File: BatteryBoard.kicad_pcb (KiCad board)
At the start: 4 copper layers, 18 parts, among them SW1 SW_SPST, U1 BQ25619ERTWR

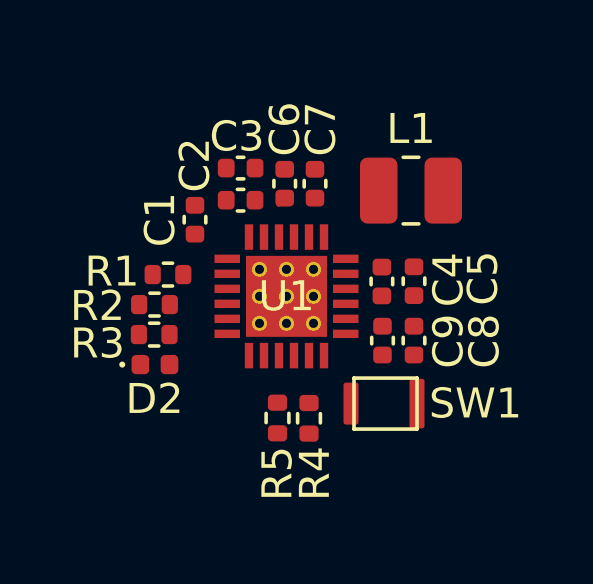
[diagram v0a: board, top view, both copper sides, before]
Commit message: Board Outline and placement Completed
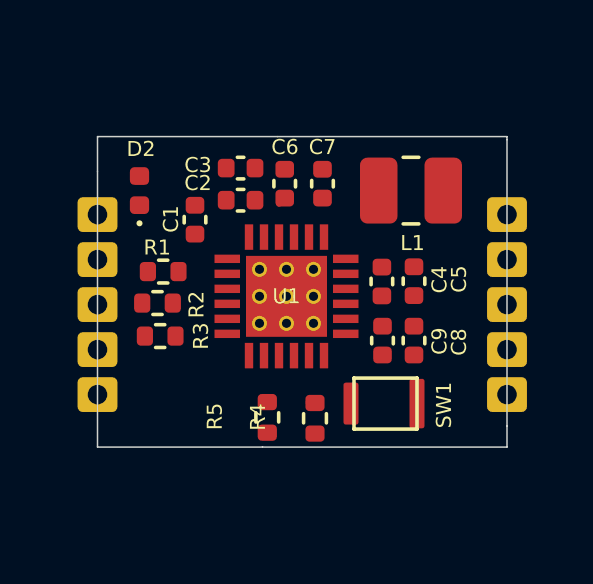
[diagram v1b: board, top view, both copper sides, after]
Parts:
- added J1: Conn_01x05_Pin, Library:5_Castellated, F.Cu at (67.1, 43.4)
- added J2: Conn_01x05_Pin, Library:5_Castellated, F.Cu at (80.8, 43.4)
- moved D2 5.82 mm to (68.5, 42.6), turned to 90 degrees
- moved R5 0.34 mm to (72.8, 50.2)
- moved C7 0.25 mm to (74.6, 42.4), turned to 90 degrees
- moved R3 0.21 mm to (69.2, 47.5)
- moved R4 0.20 mm to (74.3, 50.2)
- moved R1 0.19 mm to (69.3, 45.3)
- moved R2 0.11 mm to (69.1, 46.4)
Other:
- board outline added: 13.7 x 10.4 mm

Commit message: Minor Update for Routing
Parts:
- removed D2: LED, LED_SMD:LED_0402_1005Metric
- removed R3: 10k, Resistor_SMD:R_0402_1005Metric
- moved R4 1.98 mm to (72.4, 50.0), turned to 0 degrees
- moved R5 1.57 mm to (74.3, 50.0), turned to 0 degrees
- moved R2 1.23 mm to (69.5, 47.5), turned to -90 degrees
- moved J1 0.50 mm to (67.6, 43.4)
- moved R1 0.34 mm to (69.6, 45.5), turned to -90 degrees
- moved SW1 0.21 mm to (77.9, 49.6)
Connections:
- U1 pad 3: /PG -> unconnected-(U1-PMID_GOOD-Pad3)
- U1 pad 4: /STAT -> unconnected-(U1-STAT-Pad4)
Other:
- board size 13.7 x 10.4 mm -> 13.2 x 10.4 mm

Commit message: Out to Review
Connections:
- C7 pad 1: Net-(C7-Pad1) -> /SW
- J2 pad 4: Net-(J2-Pin_4) -> /BUTTON
- J2 pad 5: /SW -> /TS_BAT
- L1 pad 1: Net-(C7-Pad1) -> /SW
- R5 pad 2: Net-(J2-Pin_4) -> /TS_BAT
- SW1 pad 2: /SW -> /BUTTON
- U1 pad 12: /SW -> /BUTTON
- U1 pad 19: Net-(C7-Pad1) -> /SW
- U1 pad 20: Net-(C7-Pad1) -> /SW
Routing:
- net /VBAT: track 0.00 -> 12.2 mm, vias 0 -> 2
- net VBUS: track 0.00 -> 12.1 mm
- net /VSYS: track 0.00 -> 10.7 mm
- net GND: track 0.00 -> 8.44 mm, vias 0 -> 11
- net /BUTTON: track 0.00 -> 8.08 mm, vias 0 -> 1
- net /SW: track 0.00 -> 7.75 mm
- net /CE_N: track 0.00 -> 6.62 mm
- net /TS_BAT: track 0.00 -> 6.61 mm, vias 0 -> 1
- net /INT_N: track 0.00 -> 5.81 mm
- net /SCL: track 0.00 -> 4.64 mm, vias 0 -> 1
- net /SDA: track 0.00 -> 4.25 mm, vias 0 -> 1
- net /PSEL: track 0.00 -> 3.11 mm
- net /TS: track 0.00 -> 2.99 mm
- net Net-(U1-BTST): track 0.00 -> 2.65 mm
- net /PMID: track 0.00 -> 2.42 mm
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- added copper zone on F.Cu, net /SW
- added copper zone on F.Cu, net /VBAT
- added copper zone on F.Cu, net /VSYS
- added copper zone on F.Cu, net GND
- added copper zone on In1.Cu, net GND
- added copper zone on In2.Cu, net GND
- added copper zone on F.Cu, net VBUS
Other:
- outline, holes or cut-outs redrawn

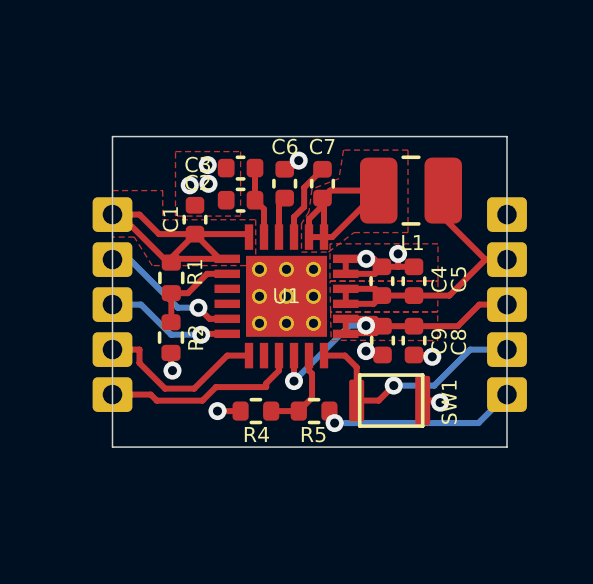
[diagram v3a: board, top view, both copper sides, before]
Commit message: Castelated edges upodate, relayout for TS Resistor
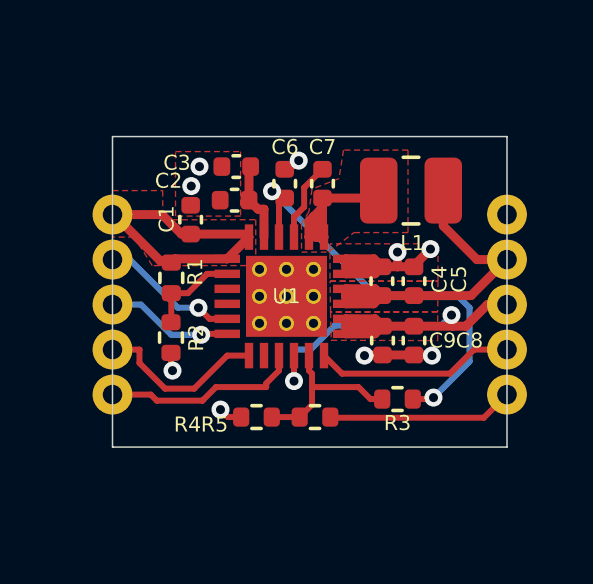
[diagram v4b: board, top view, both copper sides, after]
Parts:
- removed SW1: SW_SPST, Library:NANOT 240 AS
- added R3: 10k, Resistor_SMD:R_0402_1005Metric, F.Cu at (77.1, 49.5)
- C2, C3, C4, C5, C6, C8, C9: value 4.7u -> 10u
- moved R5 0.20 mm to (74.3, 50.1)
- moved R4 0.20 mm to (72.4, 50.1)
- moved C2 0.20 mm to (71.7, 42.9)
- moved C3 0.15 mm to (71.7, 41.8)
- moved C1 0.14 mm to (70.2, 43.6)
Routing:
- net /REGN: track 1.38 -> 14.3 mm, vias 0 -> 2
- net /VBAT: track 12.2 -> 16.9 mm
- net /TS: track 2.99 -> 5.70 mm
- net GND: track 8.44 -> 11.0 mm, vias 11 -> 9
- net /VSYS: track 10.7 -> 12.8 mm
- net /SW: track 7.75 -> 6.01 mm
- net VBUS: track 12.1 -> 10.5 mm
- net /BUTTON: track 8.08 -> 6.68 mm, vias 1 -> 0
- net /TS_BAT: track 6.61 -> 6.22 mm, vias 1 -> 0

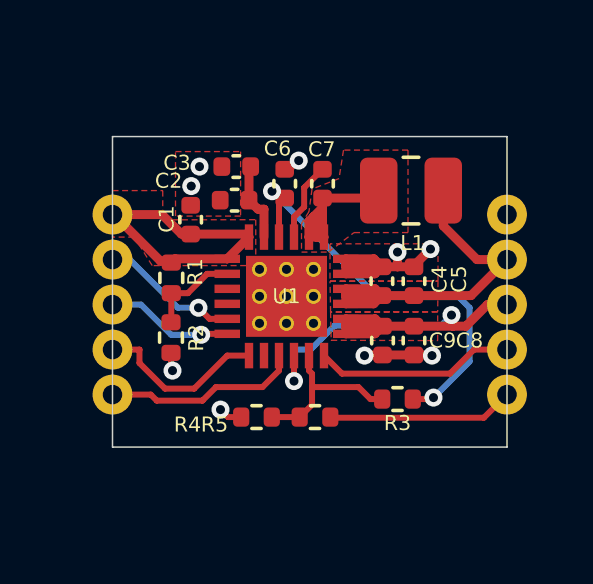
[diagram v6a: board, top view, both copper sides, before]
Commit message: Thickened Traces a little
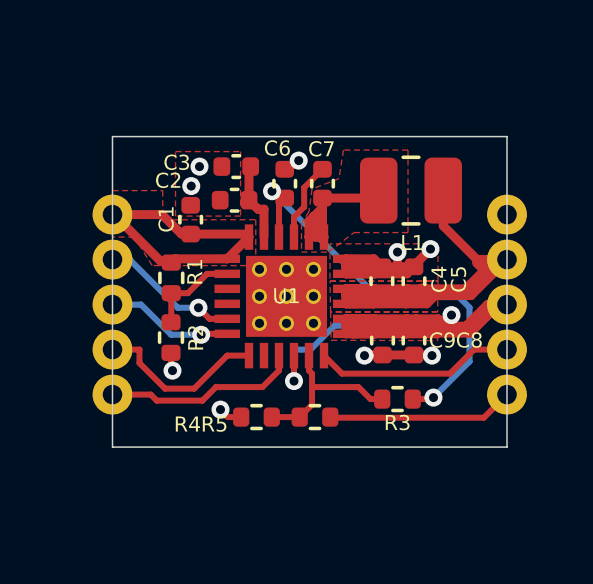
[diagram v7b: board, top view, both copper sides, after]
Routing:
- net /VBAT: track 16.9 -> 27.5 mm
- net /VSYS: track 12.8 -> 23.3 mm
- net GND: track 11.0 -> 13.3 mm

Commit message: Cleanup, and ordered boards
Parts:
- L1: value 1u -> 1uH
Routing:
- net /VSYS: track 23.3 -> 27.2 mm
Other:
- board size 13.2 x 10.4 mm -> 13.2 x 15.4 mm
